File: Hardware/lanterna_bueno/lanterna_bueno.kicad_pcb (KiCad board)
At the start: 2 copper layers, 75.1 x 56.5 mm, 51 parts, among them J1 USB_B_Micro, Q1 BC807, Q2 2SK4075, Q3 2SK4075, Q4 2SK4075, Q5 2SK4075, SW1 SW_Push, SW2 SW_Push, SW3 SW_Push, U1 RT9193-33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

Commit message: usb c
falta posicionar
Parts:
- added P1: USB_C_Plug_USB2.0, Connector_USB:USB_C_Receptacle_HRO_TYPE-C-31-M-12, F.Cu at (161.6, 94.5)
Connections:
- R10 pad 2: Net-(J1-Pad1) -> Net-(R10-Pad2)
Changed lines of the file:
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@@
   (net 63 "unconnected-(U4-Pad24)")
   (net 64 "unconnected-(U4-Pad25)")
+  (net 65 "Net-(R10-Pad2)")
+  (net 66 "unconnected-(P1-PadA5)")
+  (net 67 "unconnected-(P1-PadA6)")
+  (net 68 "unconnected-(P1-PadA7)")
+  (net 69 "unconnected-(P1-PadB5)")
   (footprint "Capacitor_SMD:CP_Elec_4x3" (layer "F.Cu")
     (at 145.6612 91.864)
@@
       (net 41 "Net-(C6-Pad1)") (pintype "passive"))
     (pad "2" smd roundrect (at 0.825 0) (size 0.8 0.95) (layers "F.Cu" "F.Paste" "F.Mask") (roundrect_rratio 0.25)
-      (net 48 "Net-(J1-Pad1)") (pintype "passive"))
+      (net 65 "Net-(R10-Pad2)") (pintype "passive"))
     (model "${KICAD6_3DMODEL_DIR}/Resistor_SMD.3dshapes/R_0603_1608Metric.wrl"
       (offset (xyz 0 0 0))
@@
     (pad "" np_thru_hole circle (at 0 0) (size 3.2 3.2) (drill 3.2) (layers *.Cu *.Mask))
   )
+  (footprint "Connector_USB:USB_C_Receptacle_HRO_TYPE-C-31-M-12" (layer "F.Cu")
+    (at 161.5616 94.4548 90)
+    (descr "USB Type-C receptacle for USB 2.0 and PD, http://www.krhro.com/uploads/soft/180320/1-1P320120243.pdf")
+    (tags "usb usb-c 2.0 pd")
+    (property "Sheetfile" "lanterna_bueno.kicad_sch")
+    (property "Sheetname" "")
+    (attr smd)
+    (fp_text reference "P1" (at 0 -5.645 90) (layer "F.SilkS")
+      (effects (font (size 1 1) (thickness 0.15)))
+    )
+    (fp_text value "USB_C_Plug_USB2.0" (at 0 5.1 90) (layer "F.Fab")
+      (effects (font (size 1 1) (thickness 0.15)))
+    )
+    (fp_text user "${REFERENCE}" (at 0 0 90) (layer "F.Fab")
+      (effects (font (size 1 1) (thickness 0.15)))
+    )
+    (fp_line (start 4.7 -1.9) (end 4.7 0.1) (layer "F.SilkS") (width 0.12))
+    (fp_line (start -4.7 -1.9) (end -4.7 0.1) (layer "F.SilkS") (width 0.12))
+    (fp_line (start 4.7 2) (end 4.7 3.9) (layer "F.SilkS") (width 0.12))
+    (fp_line (start -4.7 3.9) (end 4.7 3.9) (layer "F.SilkS") (width 0.12))
+    (fp_line (start -4.7 2) (end -4.7 3.9) (layer "F.SilkS") (width 0.12))
+    (fp_line (start -5.32 4.15) (end 5.32 4.15) (layer "F.CrtYd") (width 0.05))
+    (fp_line (start -5.32 -5.27) (end 5.32 -5.27) (layer "F.CrtYd") (width 0.05))
+    (fp_line (start -5.32 -5.27) (end -5.32 4.15) (layer "F.CrtYd") (width 0.05))
+    (fp_line (start 5.32 -5.27) (end 5.32 4.15) (layer "F.CrtYd") (width 0.05))
+    (fp_line (start 4.47 -3.65) (end 4.47 3.65) (layer "F.Fab") (width 0.1))
+    (fp_line (start -4.47 3.65) (end 4.47 3.65) (layer "F.Fab") (width 0.1))
+    (fp_line (start -4.47 -3.65) (end 4.47 -3.65) (layer "F.Fab") (width 0.1))
+    (fp_line (start -4.47 -3.65) (end -4.47 3.65) (layer "F.Fab") (width 0.1))
+    (pad "" np_thru_hole circle (at 2.89 -2.6 90) (size 0.65 0.65) (drill 0.65) (layers *.Cu *.Mask))
+    (pad "" np_thru_hole circle (at -2.89 -2.6 90) (size 0.65 0.65) (drill 0.65) (layers *.Cu *.Mask))
+    (pad "A1" smd rect (at -3.25 -4.045 90) (size 0.6 1.45) (layers "F.Cu" "F.Paste" "F.Mask")
+      (net 6 "GND") (pinfunction "GND") (pintype "passive"))
+    (pad "A4" smd rect (at -2.45 -4.045 90) (size 0.6 1.45) (layers "F.Cu" "F.Paste" "F.Mask")
+      (net 65 "Net-(R10-Pad2)") (pinfunction "VBUS") (pintype "passive"))
+    (pad "A5" smd rect (at -1.25 -4.045 90) (size 0.3 1.45) (layers "F.Cu" "F.Paste" "F.Mask")
+      (net 66 "unconnected-(P1-PadA5)") (pinfunction "CC") (pintype "bidirectional"))
+    (pad "A6" smd rect (at -0.25 -4.045 90) (size 0.3 1.45) (layers "F.Cu" "F.Paste" "F.Mask")
+      (net 67 "unconnected-(P1-PadA6)") (pinfunction "D+") (pintype "bidirectional"))
+    (pad "A7" smd rect (at 0.25 -4.045 90) (size 0.3 1.45) (layers "F.Cu" "F.Paste" "F.Mask")
+      (net 68 "unconnected-(P1-PadA7)") (pinfunction "D-") (pintype "bidirectional"))
+    (pad "A8" smd rect (at 1.25 -4.045 90) (size 0.3 1.45) (layers "F.Cu" "F.Paste" "F.Mask"))
+    (pad "A9" smd rect (at 2.45 -4.045 90) (size 0.6 1.45) (layers "F.Cu" "F.Paste" "F.Mask")
+      (net 65 "Net-(R10-Pad2)") (pinfunction "VBUS") (pintype "passive"))
+    (pad "A12" smd rect (at 3.25 -4.045 90) (size 0.6 1.45) (layers "F.Cu" "F.Paste" "F.Mask")
+      (net 6 "GND") (pinfunction "GND") (pintype "passive"))
+    (pad "B1" smd rect (at 3.25 -4.045 90) (size 0.6 1.45) (layers "F.Cu" "F.Paste" "F.Mask")
+      (net 6 "GND") (pinfunction "GND") (pintype "passive"))
+    (pad "B4" smd rect (at 2.45 -4.045 90) (size 0.6 1.45) (layers "F.Cu" "F.Paste" "F.Mask")
+      (net 65 "Net-(R10-Pad2)") (pinfunction "VBUS") (pintype "passive"))
+    (pad "B5" smd rect (at 1.75 -4.045 90) (size 0.3 1.45) (layers "F.Cu" "F.Paste" "F.Mask")
+      (net 69 "unconnected-(P1-PadB5)") (pinfunction "VCONN") (pintype "bidirectional"))
+    (pad "B6" smd rect (at 0.75 -4.045 90) (size 0.3 1.45) (layers "F.Cu" "F.Paste" "F.Mask"))
+    (pad "B7" smd rect (at -0.75 -4.045 90) (size 0.3 1.45) (layers "F.Cu" "F.Paste" "F.Mask"))
+    (pad "B8" smd rect (at -1.75 -4.045 90) (size 0.3 1.45) (layers "F.Cu" "F.Paste" "F.Mask"))
+    (pad "B9" smd rect (at -2.45 -4.045 90) (size 0.6 1.45) (layers "F.Cu" "F.Paste" "F.Mask")
+      (net 65 "Net-(R10-Pad2)") (pinfunction "VBUS") (pintype "passive"))
+    (pad "B12" smd rect (at -3.25 -4.045 90) (size 0.6 1.45) (layers "F.Cu" "F.Paste" "F.Mask")
+      (net 6 "GND") (pinfunction "GND") (pintype "passive"))
+    (pad "S1" thru_hole oval (at 4.32 1.05 90) (size 1 1.6) (drill oval 0.6 1.2) (layers *.Cu *.Mask)
+      (net 6 "GND") (pinfunction "SHIELD") (pintype "passive"))
+    (pad "S1" thru_hole oval (at -4.32 1.05 90) (size 1 1.6) (drill oval 0.6 1.2) (layers *.Cu *.Mask)
+      (net 6 "GND") (pinfunction "SHIELD") (pintype "passive"))
+    (pad "S1" thru_hole oval (at 4.32 -3.13 90) (size 1 2.1) (drill oval 0.6 1.7) (layers *.Cu *.Mask)
+      (net 6 "GND") (pinfunction "SHIELD") (pintype "passive"))
+    (pad "S1" thru_hole oval (at -4.32 -3.13 90) (size 1 2.1) (drill oval 0.6 1.7) (layers *.Cu *.Mask)
+      (net 6 "GND") (pinfunction "SHIELD") (pintype "passive"))
+    (model "${KICAD6_3DMODEL_DIR}/Connector_USB.3dshapes/USB_C_Receptacle_HRO_TYPE-C-31-M-12.wrl"
+      (offset (xyz 0 0 0))
+      (scale (xyz 1 1 1))
+      (rotate (xyz 0 0 0))
+    )
+  )
   (footprint "MountingHole:MountingHole_3.2mm_M3" (layer "F.Cu")

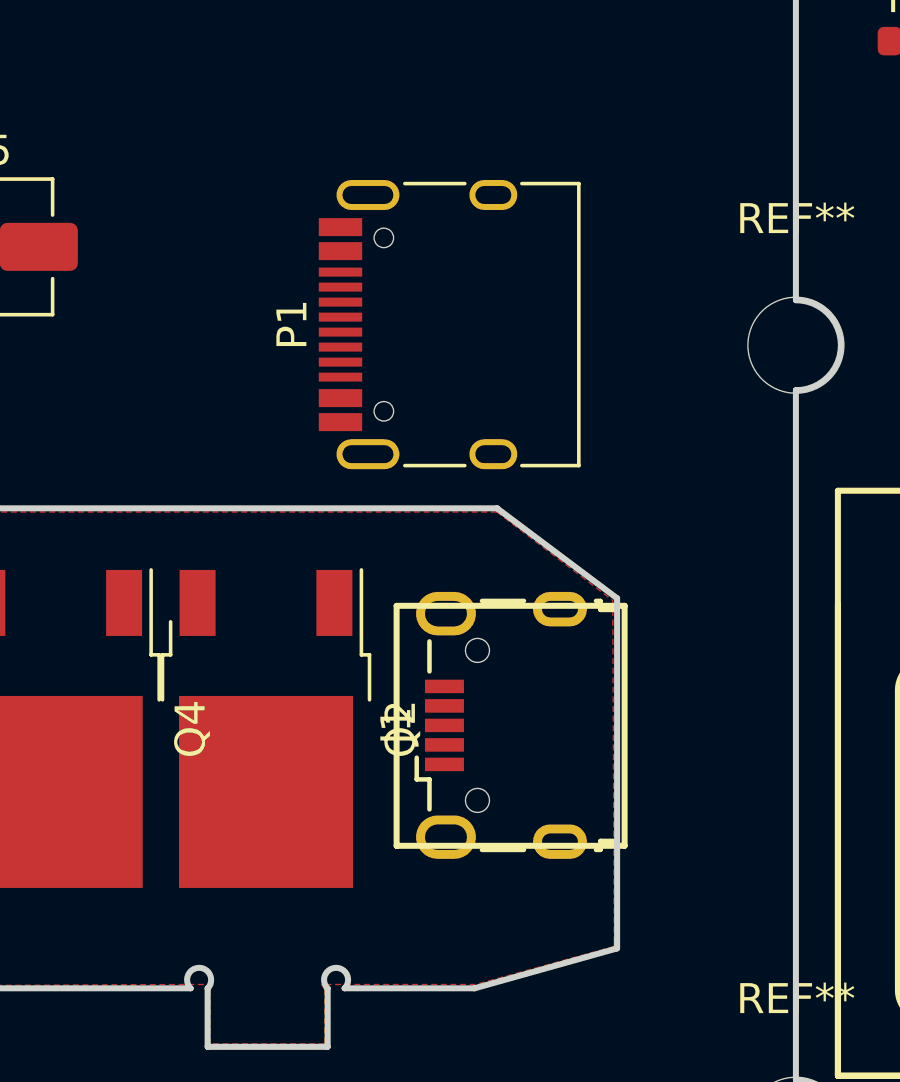
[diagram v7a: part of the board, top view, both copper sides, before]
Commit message: USB-B to USB-C
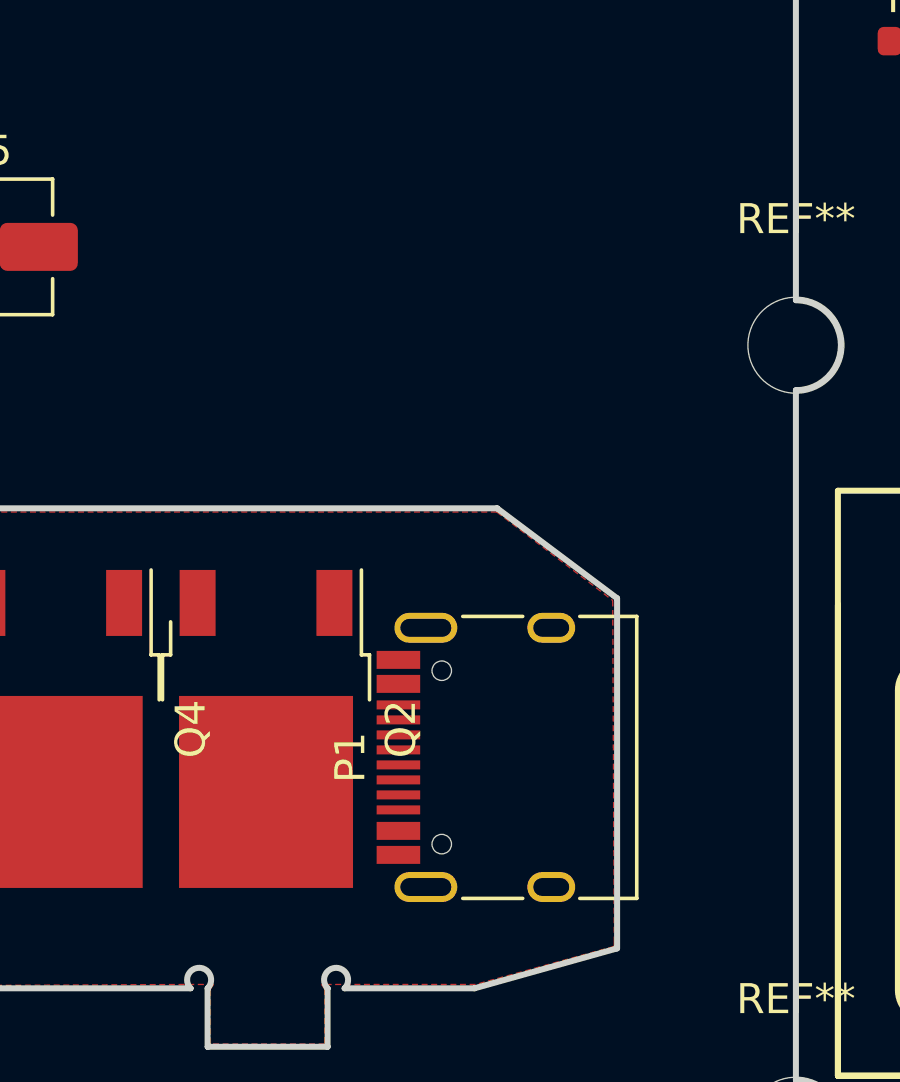
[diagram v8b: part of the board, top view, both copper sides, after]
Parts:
- removed J1: USB_B_Micro, Connector_USB:USB_Micro-B_Wuerth_629105150521
- moved P1 14.6 mm to (163.5, 108.9)
